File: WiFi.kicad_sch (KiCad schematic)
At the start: 4 parts, among them U4 AP6526, Y1 Crystal

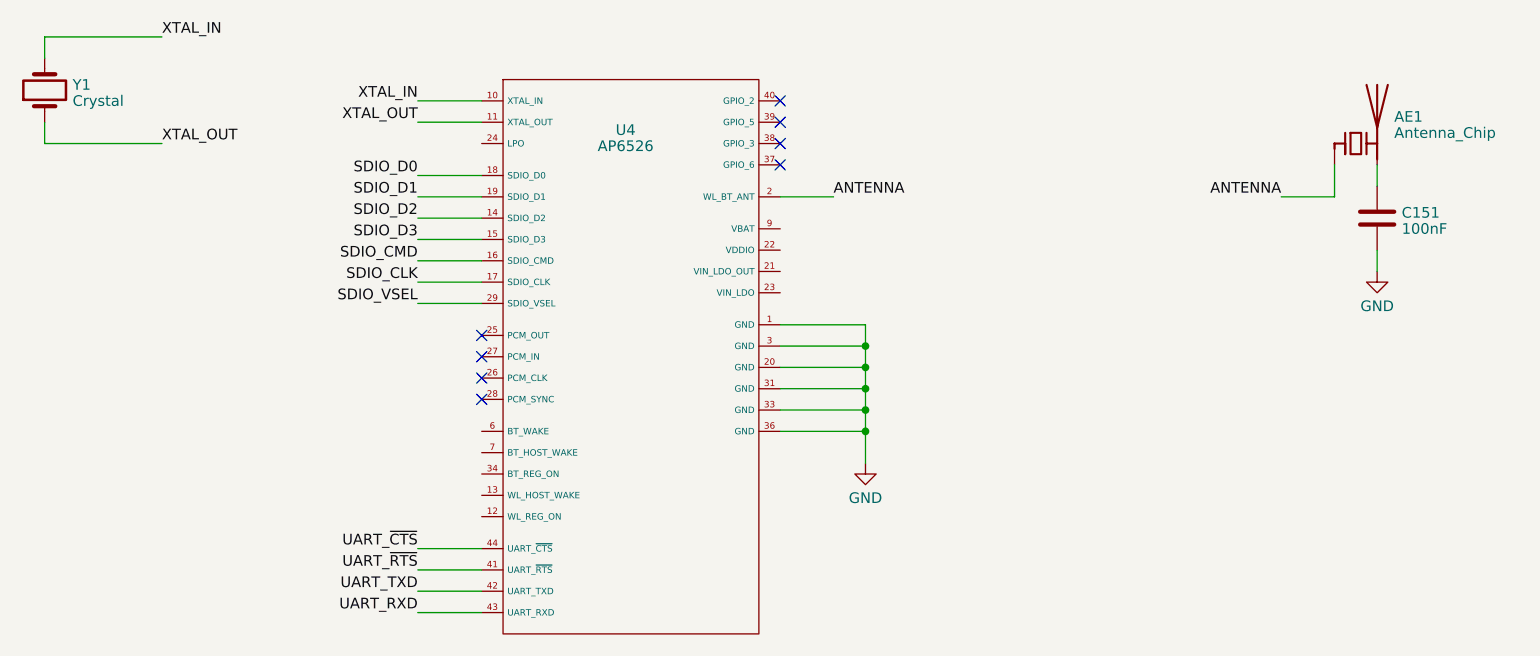
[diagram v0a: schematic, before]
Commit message: fix some ERCs
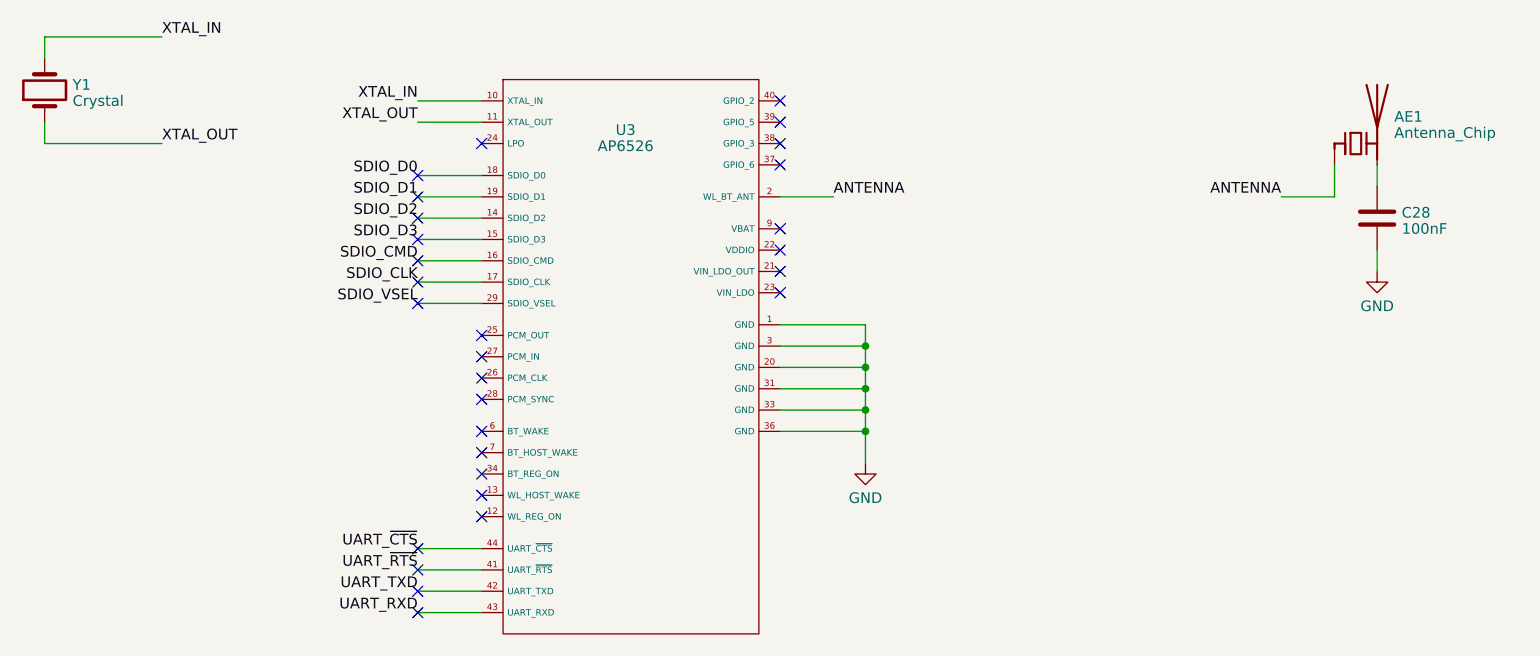
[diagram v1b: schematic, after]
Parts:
- renumbered C151 to C28, U4 to U3
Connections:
- no-connect marks 8 -> 29
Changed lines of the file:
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@@
   )
   (no_connect (at 130.81 71.12))
+  (no_connect (at 123.19 96.52))
+  (no_connect (at 166.37 66.04))
+  (no_connect (at 130.81 92.71))
+  (no_connect (at 123.19 52.07))
+  (no_connect (at 166.37 63.5))
+  (no_connect (at 123.19 62.23))
   (no_connect (at 130.81 76.2))
+  (no_connect (at 166.37 58.42))
+  (no_connect (at 130.81 87.63))
+  (no_connect (at 130.81 90.17))
+  (no_connect (at 123.19 101.6))
+  (no_connect (at 123.19 57.15))
   (no_connect (at 130.81 78.74))
+  (no_connect (at 130.81 85.09))
   (no_connect (at 130.81 73.66))
   (no_connect (at 166.37 43.18))
+  (no_connect (at 130.81 82.55))
+  (no_connect (at 123.19 64.77))
   (no_connect (at 166.37 45.72))
+  (no_connect (at 123.19 67.31))
+  (no_connect (at 123.19 54.61))
   (no_connect (at 166.37 48.26))
   (no_connect (at 166.37 50.8))
+  (no_connect (at 123.19 99.06))
+  (no_connect (at 130.81 48.26))
+  (no_connect (at 166.37 60.96))
+  (no_connect (at 123.19 59.69))
+  (no_connect (at 123.19 104.14))
   (wire (pts (xy 123.19 104.14) (xy 130.81 104.14))
     (stroke (width 0) (type default))
@@
   (symbol (lib_id "Leaf_RF_Wifi:AP6256") (at 148.59 73.66 0) (unit 1)
     (in_bom no) (on_board no) (dnp no) (fields_autoplaced)
-    (property "Reference" "U4" (at 147.955 46.6471 0)
+    (property "Reference" "U3" (at 147.955 46.6471 0)
       (effects (font (size 1.27 1.27)))
     )
@@
       (project "leaf"
         (path "/e3b58043-16a3-43c8-9fad-9c9784eebfa4/cbba8301-b827-481f-8620-b434aac08349"
-          (reference "U4") (unit 1)
+          (reference "U3") (unit 1)
         )
       )
@@
   (symbol (lib_id "power:GND") (at 237.49 63.5 0) (unit 1)
     (in_bom yes) (on_board yes) (dnp no) (fields_autoplaced)
-    (property "Reference" "#PWR0136" (at 237.49 69.85 0)
+    (property "Reference" "#PWR044" (at 237.49 69.85 0)
       (effects (font (size 1.27 1.27)) hide)
     )
@@
       (project "leaf"
         (path "/e3b58043-16a3-43c8-9fad-9c9784eebfa4/cbba8301-b827-481f-8620-b434aac08349"
-          (reference "#PWR0136") (unit 1)
+          (reference "#PWR044") (unit 1)
         )
       )
@@
   (symbol (lib_id "Device:C") (at 237.49 57.15 0) (unit 1)
     (in_bom yes) (on_board yes) (dnp no) (fields_autoplaced)
-    (property "Reference" "C151" (at 240.411 56.5063 0)
+    (property "Reference" "C28" (at 240.411 56.5063 0)
       (effects (font (size 1.27 1.27)) (justify left))
     )
@@
       (project "leaf"
         (path "/e3b58043-16a3-43c8-9fad-9c9784eebfa4/cbba8301-b827-481f-8620-b434aac08349"
-          (reference "C151") (unit 1)
+          (reference "C28") (unit 1)
         )
       )
@@
   (symbol (lib_id "power:GND") (at 176.53 86.36 0) (unit 1)
     (in_bom yes) (on_board yes) (dnp no) (fields_autoplaced)
-    (property "Reference" "#PWR045" (at 176.53 92.71 0)
+    (property "Reference" "#PWR043" (at 176.53 92.71 0)
       (effects (font (size 1.27 1.27)) hide)
     )
@@
       (project "leaf"
         (path "/e3b58043-16a3-43c8-9fad-9c9784eebfa4/cbba8301-b827-481f-8620-b434aac08349"
-          (reference "#PWR045") (unit 1)
-        )
-      )
+          (reference "#PWR043") (unit 1)
+        )
+      )

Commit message: updated symbols
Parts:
- AE1, C28, Y1: now not fitted; now left out of the parts list
- U3: now not fitted
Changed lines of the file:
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@@
   )
   (symbol (lib_id "Device:Crystal") (at 78.74 41.91 90) (unit 1)
-    (in_bom yes) (on_board yes) (dnp no) (fields_autoplaced)
+    (in_bom no) (on_board no) (dnp yes) (fields_autoplaced)
     (property "Reference" "Y1" (at 82.0674 41.2663 90)
       (effects (font (size 1.27 1.27)) (justify right))
@@
   )
   (symbol (lib_id "Leaf_RF_Wifi:AP6256") (at 148.59 73.66 0) (unit 1)
-    (in_bom no) (on_board no) (dnp no) (fields_autoplaced)
+    (in_bom no) (on_board no) (dnp yes) (fields_autoplaced)
     (property "Reference" "U3" (at 147.955 46.6471 0)
       (effects (font (size 1.27 1.27)))
@@
   )
   (symbol (lib_id "Device:Antenna_Chip") (at 234.95 48.26 0) (unit 1)
-    (in_bom yes) (on_board yes) (dnp no) (fields_autoplaced)
+    (in_bom no) (on_board no) (dnp yes) (fields_autoplaced)
     (property "Reference" "AE1" (at 239.522 45.0763 0)
       (effects (font (size 1.27 1.27)) (justify left))
@@
   )
   (symbol (lib_id "Device:C") (at 237.49 57.15 0) (unit 1)
-    (in_bom yes) (on_board yes) (dnp no) (fields_autoplaced)
+    (in_bom no) (on_board no) (dnp yes) (fields_autoplaced)
     (property "Reference" "C28" (at 240.411 56.5063 0)
       (effects (font (size 1.27 1.27)) (justify left))

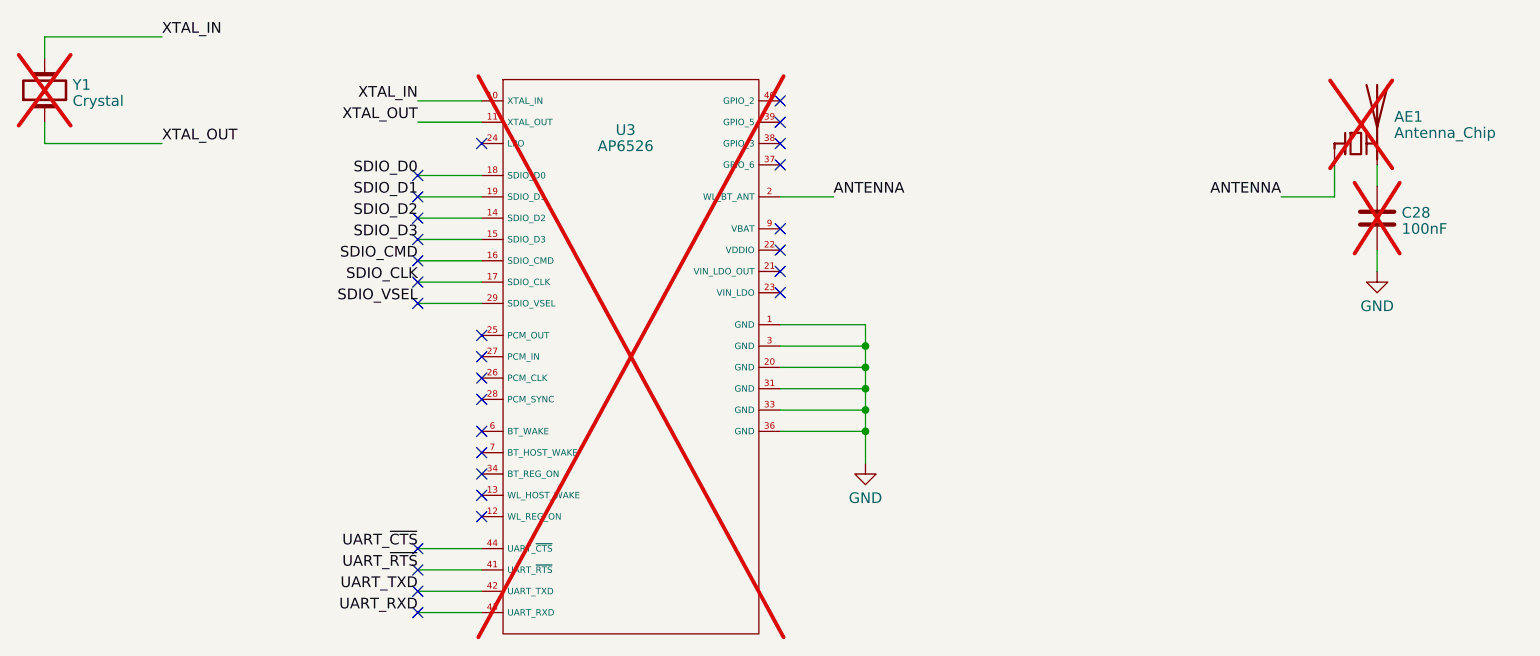
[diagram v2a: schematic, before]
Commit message: added OSC, updated annotations
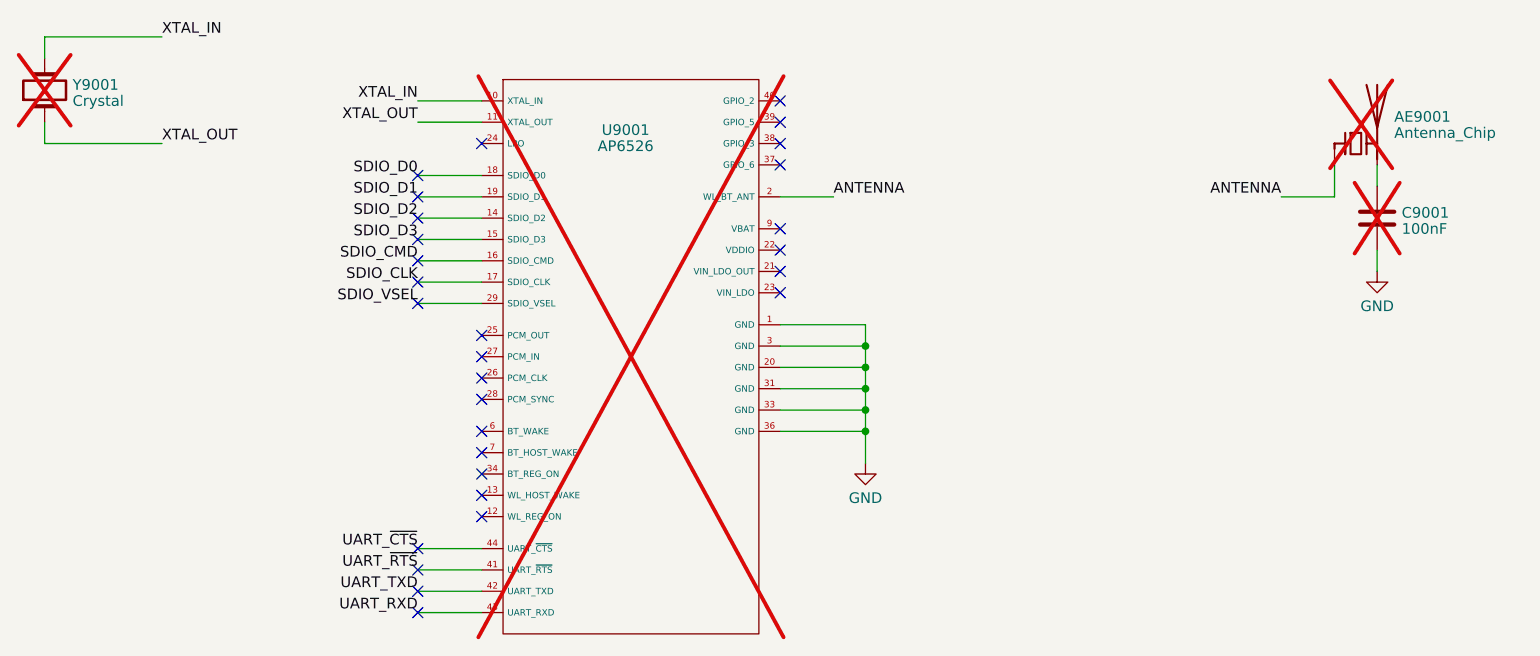
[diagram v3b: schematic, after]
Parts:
- renumbered AE1 to AE9001, C28 to C9001, U3 to U9001, Y1 to Y9001
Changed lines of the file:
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@@
   (symbol (lib_id "Device:Crystal") (at 78.74 41.91 90) (unit 1)
     (in_bom no) (on_board no) (dnp yes) (fields_autoplaced)
-    (property "Reference" "Y1" (at 82.0674 41.2663 90)
+    (property "Reference" "Y9001" (at 82.0674 41.2663 90)
       (effects (font (size 1.27 1.27)) (justify right))
     )
@@
       (project "leaf"
         (path "/e3b58043-16a3-43c8-9fad-9c9784eebfa4/cbba8301-b827-481f-8620-b434aac08349"
-          (reference "Y1") (unit 1)
+          (reference "Y9001") (unit 1)
         )
       )
@@
   (symbol (lib_id "Leaf_RF_Wifi:AP6256") (at 148.59 73.66 0) (unit 1)
     (in_bom no) (on_board no) (dnp yes) (fields_autoplaced)
-    (property "Reference" "U3" (at 147.955 46.6471 0)
+    (property "Reference" "U9001" (at 147.955 46.6471 0)
       (effects (font (size 1.27 1.27)))
     )
@@
       (project "leaf"
         (path "/e3b58043-16a3-43c8-9fad-9c9784eebfa4/cbba8301-b827-481f-8620-b434aac08349"
-          (reference "U3") (unit 1)
+          (reference "U9001") (unit 1)
         )
       )
@@
   (symbol (lib_id "Device:Antenna_Chip") (at 234.95 48.26 0) (unit 1)
     (in_bom no) (on_board no) (dnp yes) (fields_autoplaced)
-    (property "Reference" "AE1" (at 239.522 45.0763 0)
+    (property "Reference" "AE9001" (at 239.522 45.0763 0)
       (effects (font (size 1.27 1.27)) (justify left))
     )
@@
       (project "leaf"
         (path "/e3b58043-16a3-43c8-9fad-9c9784eebfa4/cbba8301-b827-481f-8620-b434aac08349"
-          (reference "AE1") (unit 1)
+          (reference "AE9001") (unit 1)
         )
       )
@@
   (symbol (lib_id "power:GND") (at 237.49 63.5 0) (unit 1)
     (in_bom yes) (on_board yes) (dnp no) (fields_autoplaced)
-    (property "Reference" "#PWR044" (at 237.49 69.85 0)
+    (property "Reference" "#PWR09002" (at 237.49 69.85 0)
       (effects (font (size 1.27 1.27)) hide)
     )
@@
       (project "leaf"
         (path "/e3b58043-16a3-43c8-9fad-9c9784eebfa4/cbba8301-b827-481f-8620-b434aac08349"
-          (reference "#PWR044") (unit 1)
+          (reference "#PWR09002") (unit 1)
         )
       )
@@
   (symbol (lib_id "Device:C") (at 237.49 57.15 0) (unit 1)
     (in_bom no) (on_board no) (dnp yes) (fields_autoplaced)
-    (property "Reference" "C28" (at 240.411 56.5063 0)
+    (property "Reference" "C9001" (at 240.411 56.5063 0)
       (effects (font (size 1.27 1.27)) (justify left))
     )
@@
       (project "leaf"
         (path "/e3b58043-16a3-43c8-9fad-9c9784eebfa4/cbba8301-b827-481f-8620-b434aac08349"
-          (reference "C28") (unit 1)
+          (reference "C9001") (unit 1)
         )
       )
@@
   (symbol (lib_id "power:GND") (at 176.53 86.36 0) (unit 1)
     (in_bom yes) (on_board yes) (dnp no) (fields_autoplaced)
-    (property "Reference" "#PWR043" (at 176.53 92.71 0)
+    (property "Reference" "#PWR09001" (at 176.53 92.71 0)
       (effects (font (size 1.27 1.27)) hide)
     )
@@
       (project "leaf"
         (path "/e3b58043-16a3-43c8-9fad-9c9784eebfa4/cbba8301-b827-481f-8620-b434aac08349"
-          (reference "#PWR043") (unit 1)
+          (reference "#PWR09001") (unit 1)
         )
       )

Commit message: move DDR power decoupling capacitors into DDR4 Sheet
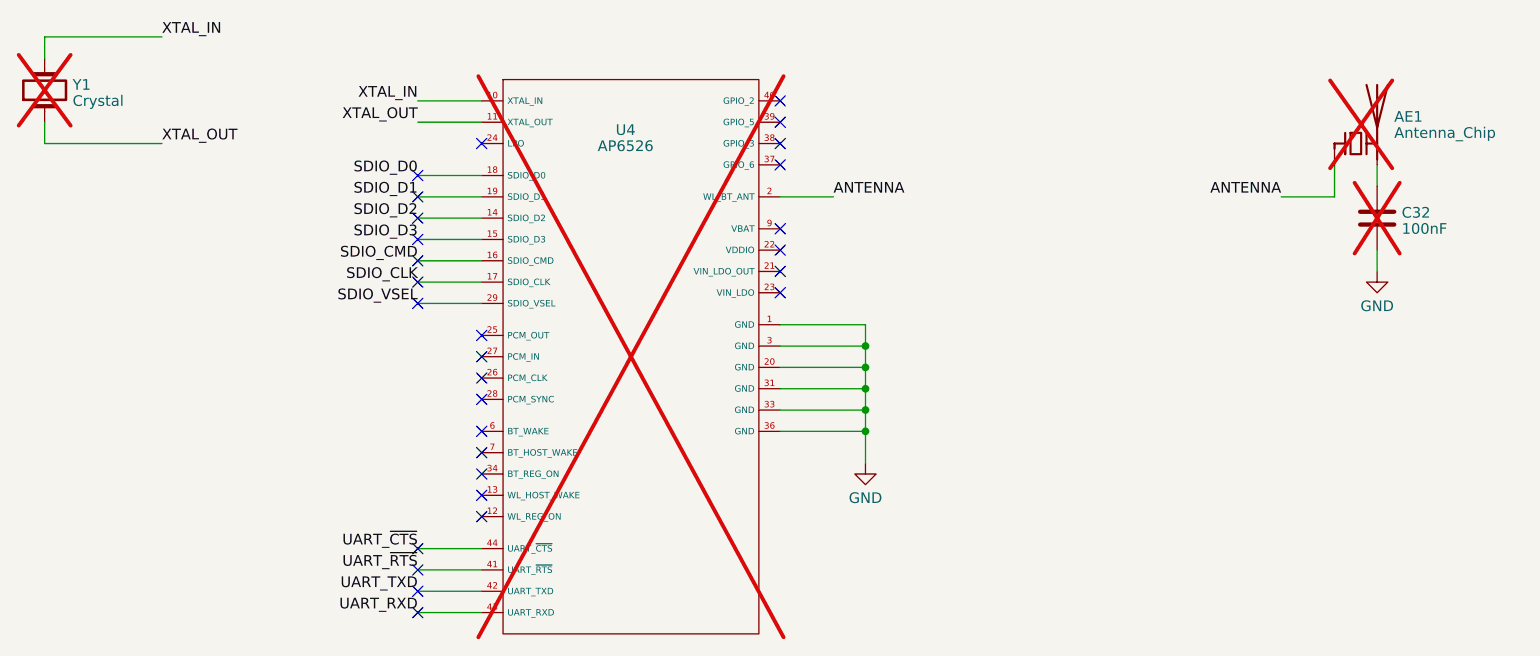
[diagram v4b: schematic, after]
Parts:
- renumbered AE9001 to AE1, C9001 to C32, U9001 to U4, Y9001 to Y1
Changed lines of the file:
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@@
   (symbol (lib_id "Device:Crystal") (at 78.74 41.91 90) (unit 1)
     (in_bom no) (on_board no) (dnp yes) (fields_autoplaced)
-    (property "Reference" "Y9001" (at 82.0674 41.2663 90)
+    (property "Reference" "Y1" (at 82.0674 41.2663 90)
       (effects (font (size 1.27 1.27)) (justify right))
     )
@@
       (project "leaf"
         (path "/e3b58043-16a3-43c8-9fad-9c9784eebfa4/cbba8301-b827-481f-8620-b434aac08349"
-          (reference "Y9001") (unit 1)
+          (reference "Y1") (unit 1)
         )
       )
@@
   (symbol (lib_id "Leaf_RF_Wifi:AP6256") (at 148.59 73.66 0) (unit 1)
     (in_bom no) (on_board no) (dnp yes) (fields_autoplaced)
-    (property "Reference" "U9001" (at 147.955 46.6471 0)
+    (property "Reference" "U4" (at 147.955 46.6471 0)
       (effects (font (size 1.27 1.27)))
     )
@@
       (project "leaf"
         (path "/e3b58043-16a3-43c8-9fad-9c9784eebfa4/cbba8301-b827-481f-8620-b434aac08349"
-          (reference "U9001") (unit 1)
+          (reference "U4") (unit 1)
         )
       )
@@
   (symbol (lib_id "Device:Antenna_Chip") (at 234.95 48.26 0) (unit 1)
     (in_bom no) (on_board no) (dnp yes) (fields_autoplaced)
-    (property "Reference" "AE9001" (at 239.522 45.0763 0)
+    (property "Reference" "AE1" (at 239.522 45.0763 0)
       (effects (font (size 1.27 1.27)) (justify left))
     )
@@
       (project "leaf"
         (path "/e3b58043-16a3-43c8-9fad-9c9784eebfa4/cbba8301-b827-481f-8620-b434aac08349"
-          (reference "AE9001") (unit 1)
+          (reference "AE1") (unit 1)
         )
       )
@@
   (symbol (lib_id "power:GND") (at 237.49 63.5 0) (unit 1)
     (in_bom yes) (on_board yes) (dnp no) (fields_autoplaced)
-    (property "Reference" "#PWR09002" (at 237.49 69.85 0)
+    (property "Reference" "#PWR040" (at 237.49 69.85 0)
       (effects (font (size 1.27 1.27)) hide)
     )
@@
       (project "leaf"
         (path "/e3b58043-16a3-43c8-9fad-9c9784eebfa4/cbba8301-b827-481f-8620-b434aac08349"
-          (reference "#PWR09002") (unit 1)
+          (reference "#PWR040") (unit 1)
         )
       )
@@
   (symbol (lib_id "Device:C") (at 237.49 57.15 0) (unit 1)
     (in_bom no) (on_board no) (dnp yes) (fields_autoplaced)
-    (property "Reference" "C9001" (at 240.411 56.5063 0)
+    (property "Reference" "C32" (at 240.411 56.5063 0)
       (effects (font (size 1.27 1.27)) (justify left))
     )
@@
       (project "leaf"
         (path "/e3b58043-16a3-43c8-9fad-9c9784eebfa4/cbba8301-b827-481f-8620-b434aac08349"
-          (reference "C9001") (unit 1)
+          (reference "C32") (unit 1)
         )
       )
@@
   (symbol (lib_id "power:GND") (at 176.53 86.36 0) (unit 1)
     (in_bom yes) (on_board yes) (dnp no) (fields_autoplaced)
-    (property "Reference" "#PWR09001" (at 176.53 92.71 0)
+    (property "Reference" "#PWR039" (at 176.53 92.71 0)
       (effects (font (size 1.27 1.27)) hide)
     )
@@
       (project "leaf"
         (path "/e3b58043-16a3-43c8-9fad-9c9784eebfa4/cbba8301-b827-481f-8620-b434aac08349"
-          (reference "#PWR09001") (unit 1)
+          (reference "#PWR039") (unit 1)
         )
       )

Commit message: added README and license
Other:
- company: Qingdao IotPi Information Technology -> Yang Hongbo
- title: Leaf RV1126 RK809 WiFi -> Leaf RV1126
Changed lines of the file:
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@@
   (paper "A4")
   (title_block
-    (title "Leaf RV1126 RK809 WiFi")
-    (date "2023-02-25")
+    (title "Leaf RV1126")
+    (date "2023-06-07")
     (rev "1")
-    (company "Qingdao IotPi Information Technology")
+    (company "Yang Hongbo")
+    (comment 1 "License: CC BY-SA")
   )
   (junction (at 176.53 72.39) (diameter 0) (color 0 0 0 0)
